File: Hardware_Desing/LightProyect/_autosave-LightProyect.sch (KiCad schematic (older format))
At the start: 10 parts, among them J1 Screw_Terminal_01x02, J2 AudioJack2_SwitchT, J3 Screw_Terminal_01x03, M1 Regulator_x_3_3, M2 DC_DC_3_5_module, M3 AudioModule, M4 MPU6050_lite, SW1 SW_Push, U1 ESP-12E

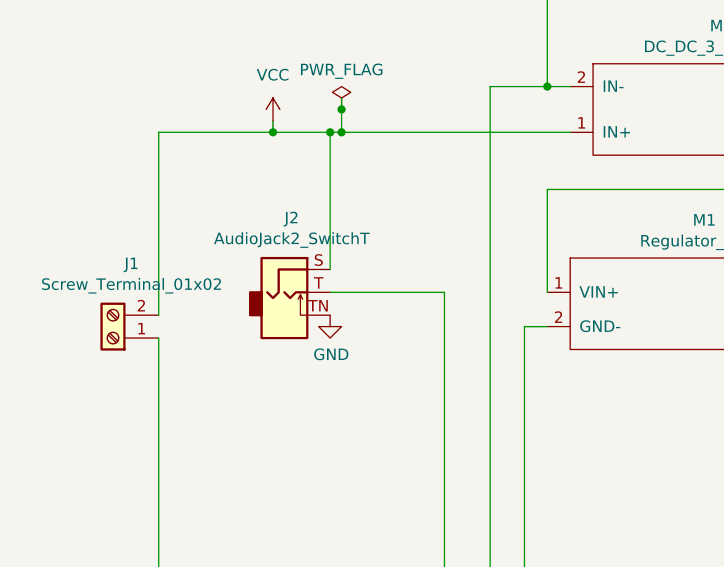
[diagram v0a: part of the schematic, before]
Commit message: PCB and Ifdef pinout
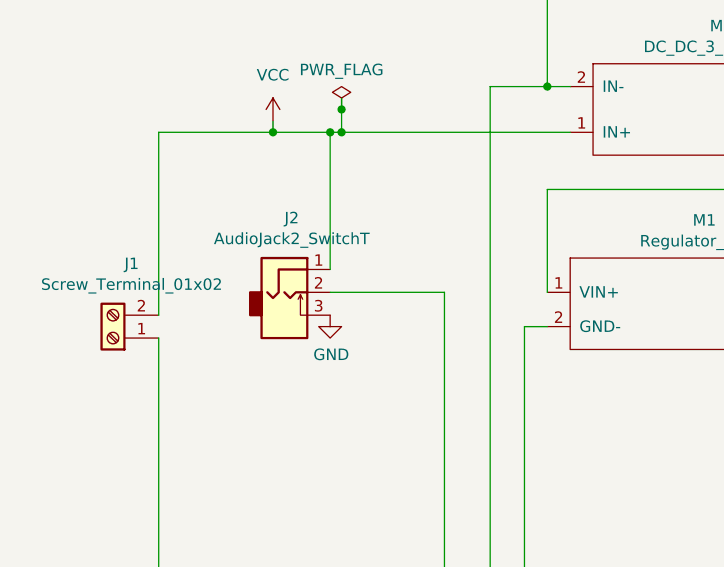
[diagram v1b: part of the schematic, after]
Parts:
- removed J2: AudioJack2_SwitchT, TerminalBlock:TerminalBlock_bornier-3_P5.08mm, symbol Connector:AudioJack2_SwitchT
- added J2: AudioJack2_SwitchT, TerminalBlock:TerminalBlock_bornier-3_P5.08mm, symbol ONOFF:AudioJack2_SwitchT
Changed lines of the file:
@@
 	0    1    1    0
-$EndComp
-$Comp
-L Connector:AudioJack2_SwitchT J2
-U 1 1 5EEB712D
-P 2000 2250
-F 0 "J2" H 2032 2575 50  0000 C CNN
-F 1 "AudioJack2_SwitchT" H 2032 2484 50  0000 C CNN
-F 2 "TerminalBlock:TerminalBlock_bornier-3_P5.08mm" H 2000 2250 50  0001 C CNN
-F 3 "~" H 2000 2250 50  0001 C CNN
-	1    2000 2250
-	1    0    0    -1
 $EndComp
 Wire Wire Line
@@
 	1    0    0    -1
 $EndComp
+$Comp
+L ONOFF:AudioJack2_SwitchT J2
+U 1 1 5EF4A436
+P 2000 2250
+F 0 "J2" H 2032 2575 50  0000 C CNN
+F 1 "AudioJack2_SwitchT" H 2032 2484 50  0000 C CNN
+F 2 "TerminalBlock:TerminalBlock_bornier-3_P5.08mm" H 2000 2250 50  0001 C CNN
+F 3 "~" H 2000 2250 50  0001 C CNN
+	1    2000 2250
+	1    0    0    -1
+$EndComp
